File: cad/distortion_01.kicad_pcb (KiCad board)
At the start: 2 copper layers, 147.5 x 81.2 mm, 103 parts, among them CON101 Ext_PSU, J101 JACK_IN, J102 JACK_OUT, P101 Battery_conn, P102 BYPASS_SWITCH, P103 CONN_01X03, P104 CONN_01X03, P105 CONN_01X03, P106 CONN_01X03, Q101 BS170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

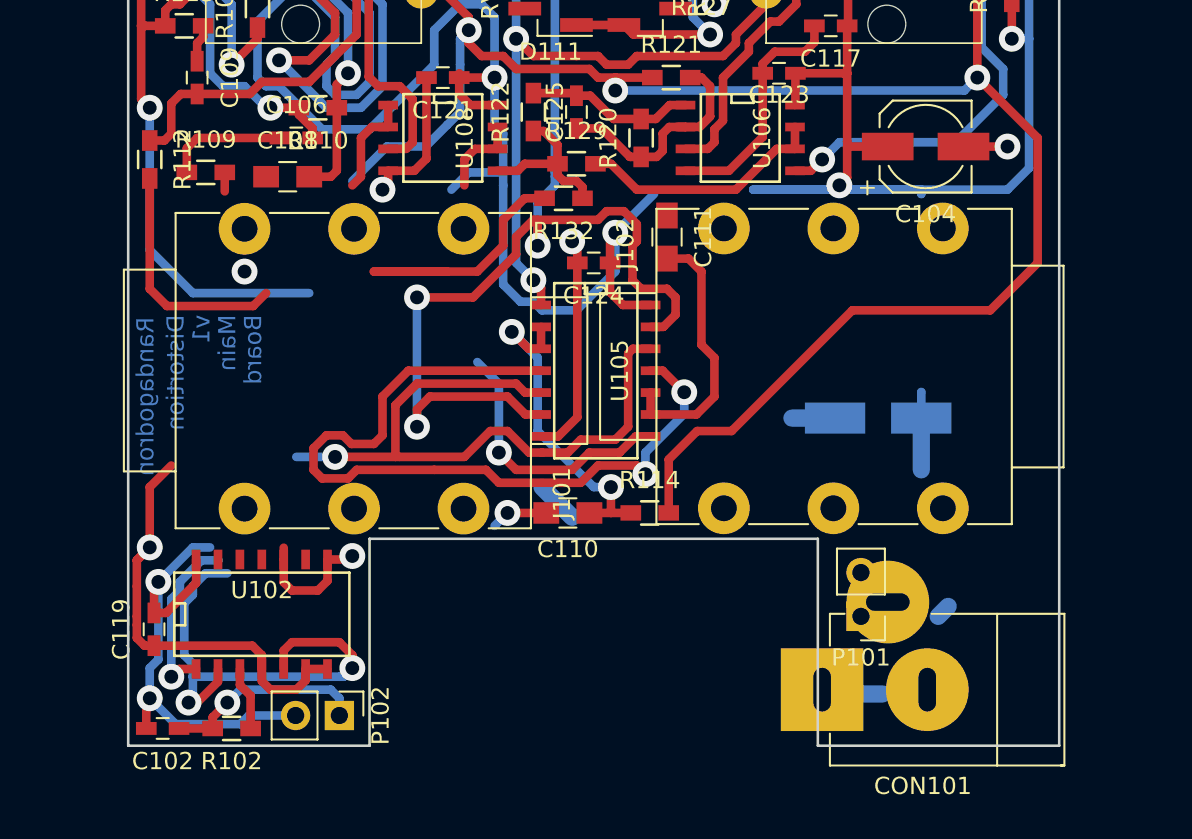
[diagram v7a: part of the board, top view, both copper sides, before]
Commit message: Changed PSU connector footprint to 3w HE10, finished layout.
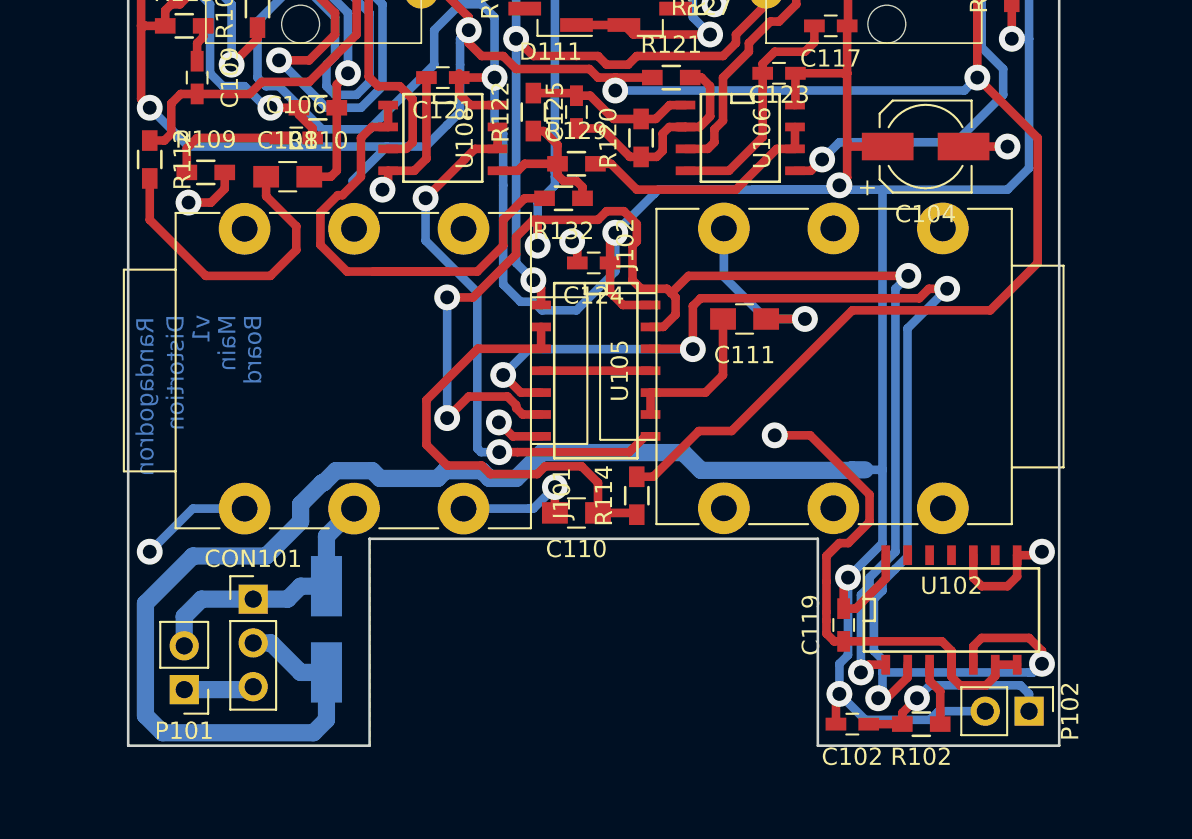
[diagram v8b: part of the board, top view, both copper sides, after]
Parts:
- CON101: footprint Connect:JACK_ALIM -> Pin_Headers:Pin_Header_Straight_1x03_Pitch2.54mm
- moved C102 40.0 mm to (82.5, 113.2)
- moved C119 40.0 mm to (82.0, 107.5)
- moved P102 40.0 mm to (92.8, 112.5)
- moved R102 40.0 mm to (86.5, 113.2)
- moved U102 40.0 mm to (88.2, 106.5)
- moved P101 39.5 mm to (43.8, 111.2)
- moved D101 34.3 mm to (52.0, 107.8), turned to 90 degrees
- moved CON101 33.4 mm to (47.8, 106.0), turned to 0 degrees
- moved C111 6.54 mm to (76.2, 89.8), turned to 180 degrees
- moved N101 4.85 mm to (83.8, 98.5), turned to 0 degrees
- moved R114 1.25 mm to (70.0, 100.0), turned to 90 degrees
- moved C110 0.50 mm to (66.5, 101.0)
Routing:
- net +BATT: track 3.00 -> 72.6 mm
- net /audio_bypass: track 46.8 -> 6.35 mm, vias 2 -> 0
- net /bypass_cmd: track 99.0 -> 124.1 mm, vias 5 -> 6
- net +9V: track 283.2 -> 299.9 mm
- net /audio_fx_out: track 20.7 -> 32.9 mm, vias 1 -> 2
- net /~bypass_cmd~: track 67.1 -> 78.9 mm, vias 3 -> 5
- net GNDPWR: track 4.35 -> 15.8 mm
- net Net-(C111-Pad1): track 0.00 -> 10.8 mm, vias 0 -> 1
- net Net-(R132-Pad2): track 22.9 -> 31.0 mm
- net /audio_jack_in: track 19.2 -> 27.0 mm, vias 2 -> 0
- net /audio_jack_out: track 15.3 -> 9.17 mm
- net VCOM: track 236.9 -> 232.2 mm
- net GND: track 148.5 -> 152.9 mm, vias 17 -> 20
- net Net-(CON101-Pad3): track 0.00 -> 4.07 mm
- net Net-(C110-Pad2): track 3.31 -> 7.32 mm
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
